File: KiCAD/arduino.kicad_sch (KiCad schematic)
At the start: 1 part, among them U2 Metro_ESP32S3

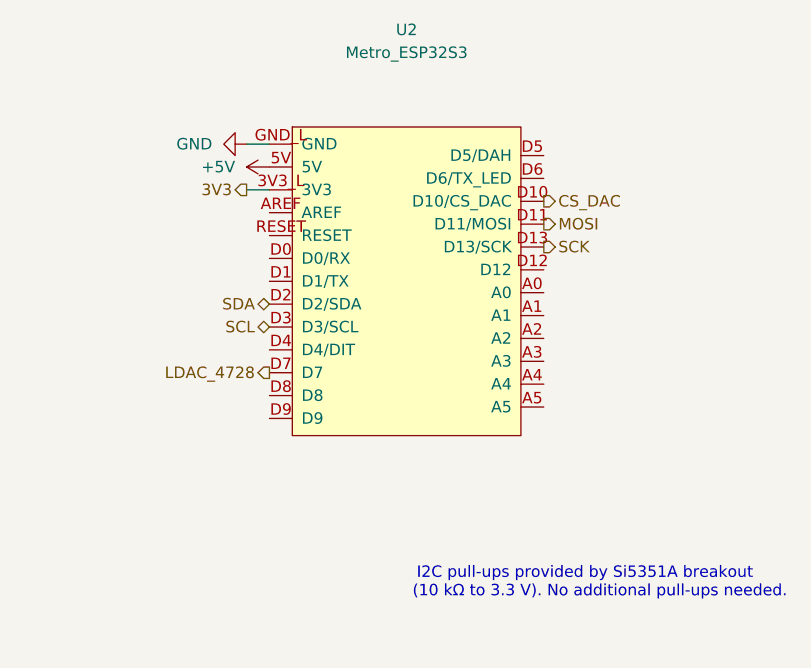
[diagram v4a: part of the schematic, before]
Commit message: kicad: re-architect I2C bus distribution via STEMMA QT to Si5351 hub
Move I2C (SDA/SCL) and +3.3V distribution from arduino-sheet-origin to
vfo-sheet-origin, matching the physical plan: STEMMA QT cable carries
I2C + 3.3V from Metro to Si5351 breakout (off-schematic), and from the
Si5351 breakout's 0.1" header the bus is distributed via PCB traces to
other I2C devices (MCP4728, future MCP23017 for LCD).

Per-file changes:

- xmitter.kicad_sym (Metro_ESP32S3 symbol): D2/D3 relabeled from
  D2/SDA, D3/SCL to D2/FREQ_A, D3/FREQ_B (input type). Aligns with
  firmware/main/pin_map.h which already uses D2/D3 for the FREQ encoder
  quadrature inputs. The real Metro's dedicated SDA/SCL pins (GPIO
  47/48) are not exposed on this custom symbol; I2C goes off-board via
  STEMMA QT.
- arduino.kicad_sch: removed SDA/SCL/3V3 hier labels (no longer the
  source of these signals). Added +3.3V power port at Metro 3V3 pin
  for ERC cleanliness. Added text note explaining STEMMA QT routing.
- vfo.kicad_sch: 3V3, SDA, SCL hier labels changed direction to output
  (Si5351 breakout is now the source).
- buffer_keyer.kicad_sch: added 3V3 (input) hier label at (48.26,
  134.62) alongside existing SDA/SCL inputs. Existing +3.3V power port
  at U8 VIN stays for now; user will need to wire the new label to
  the +3.3V net inside KiCad (or replace the power port with the label).

tools/:
- rewrite_metro_symbol.py: pin list updated, wire-deletion code
  REMOVED (it was unconditionally wiping wires on every run — only
  correct on the first conversion).
- rewire_arduino_for_stemma.py: one-shot script for the arduino sheet
  changes.
- add_3v3_label_buffer_keyer.py: one-shot script for the new 3V3 hier
  label.

Root sheet update + sheet-pin sync + cross-sheet wiring deferred to
user (needs KiCad GUI's "Import Sheet Pins" feature).
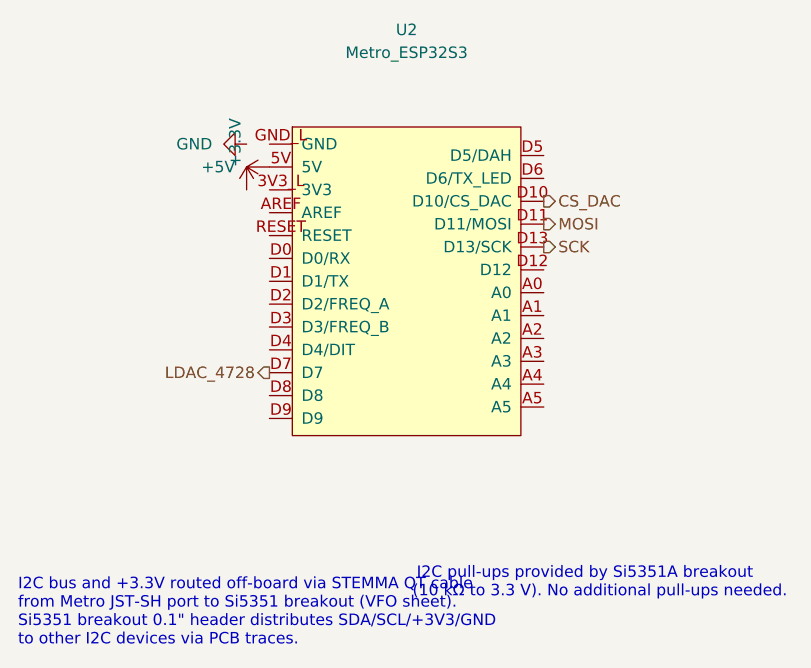
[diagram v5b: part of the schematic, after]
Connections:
- net GND: no longer U2.GND_L (GND)
- net 3V3: no longer names the net of U2.3V3_L (3V3)
- net SCL: no longer names the net of U2.D3 (D3/FREQ_B)
- net SDA: no longer names the net of U2.D2 (D2/FREQ_A)
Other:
- note added: "I2C bus and +3.3V routed off-board via STEMMA QT cable from Metro JST-SH port to Si5351 breakout (VFO sheet). Si5351 breakout 0.1" header distributes SDA/SCL/+3V3/GND to other I2C devices via PCB traces."
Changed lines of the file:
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@@
 		)
 	)
-	(wire
-		(pts
-			(xy 86.36 58.42) (xy 88.9 58.42)
-		)
-		(stroke
-			(width 0)
-			(type default)
-		)
-	)
-	(wire
-		(pts
-			(xy 86.36 63.5) (xy 88.9 63.5)
-		)
-		(stroke
-			(width 0)
-			(type default)
-		)
-	)
-	(hierarchical_label "SCL"
-		(shape bidirectional)
-		(at 88.9 78.74 180)
+	(hierarchical_label "CS_DAC"
+		(shape output)
+		(at 119.38 64.77 0)
+		(effects
+			(font
+				(size 1.27 1.27)
+			)
+			(justify left)
+		)
+	)
+	(hierarchical_label "LDAC_4728"
+		(shape output)
+		(at 88.9 83.82 180)
 		(effects
 			(font
@@
 		)
 	)
-	(hierarchical_label "SDA"
-		(shape bidirectional)
-		(at 88.9 76.2 180)
-		(effects
-			(font
-				(size 1.27 1.27)
-			)
-			(justify right)
-		)
-	)
-	(hierarchical_label "CS_DAC"
-		(shape output)
-		(at 119.38 64.77 0)
-		(effects
-			(font
-				(size 1.27 1.27)
-			)
-			(justify left)
-		)
-	)
-	(hierarchical_label "LDAC_4728"
-		(shape output)
-		(at 88.9 83.82 180)
-		(effects
-			(font
-				(size 1.27 1.27)
-			)
-			(justify right)
-		)
-	)
 	(hierarchical_label "SCK"
 		(shape output)
@@
 			)
 			(justify left)
-		)
-	)
-	(hierarchical_label "3V3"
-		(shape output)
-		(at 86.36 63.5 180)
-		(effects
-			(font
-				(size 1.27 1.27)
-			)
-			(justify right)
 		)
 	)
@@
 		)
 	)
+	(symbol
+		(lib_id "power:+3.3V")
+		(at 86.36 63.5 0)
+		(unit 1)
+		(body_style 1)
+		(exclude_from_sim no)
+		(in_bom yes)
+		(on_board yes)
+		(in_pos_files yes)
+		(dnp no)
+		(fields_autoplaced yes)
+		(property "Reference" "#PWR031"
+			(at 92.71 60.96 0)
+			(hide yes)
+			(show_name no)
+			(do_not_autoplace no)
+			(effects
+				(font
+					(size 1.27 1.27)
+				)
+			)
+		)
+		(property "Value" "+3.3V"
+			(at 85.09 60.9599 90)
+			(show_name no)
+			(do_not_autoplace no)
+			(effects
+				(font
+					(size 1.27 1.27)
+				)
+				(justify left)
+			)
+		)
+		(property "Footprint" ""
+			(at 88.9 60.96 0)
+			(hide yes)
+			(show_name no)
+			(do_not_autoplace no)
+			(effects
+				(font
+					(size 1.27 1.27)
+				)
+			)
+		)
+		(property "Datasheet" ""
+			(at 88.9 60.96 0)
+			(hide yes)
+			(show_name no)
+			(do_not_autoplace no)
+			(effects
+				(font
+					(size 1.27 1.27)
+				)
+			)
+		)
+		(property "Description" "Power symbol creates a global label with name \"+5V\""
+			(at 88.9 60.96 0)
+			(hide yes)
+			(show_name no)
+			(do_not_autoplace no)
+			(effects
+				(font
+					(size 1.27 1.27)
+				)
+			)
+		)
+		(pin "1"
+		)
+		(instances
+			(project "KiCAD"
+				(path "/d3de40b8-856b-4fbd-829c-f45ffcd55742/2d83d0b5-86d4-4ced-ab68-6465e3dc2d72"
+					(reference "#PWR030")
+					(unit 1)
+				)
+			)
+		)
+	)
+	(text "I2C bus and +3.3V routed off-board via STEMMA QT cable\nfrom Metro JST-SH port to Si5351 breakout (VFO sheet).\nSi5351 breakout 0.1\" header distributes SDA/SCL/+3V3/GND\nto other I2C devices via PCB traces."
+		(exclude_from_sim no)
+		(at 60.96 110.49 0)
+		(effects
+			(font
+				(size 1.27 1.27)
+			)
+			(justify left)
+		)
+	)
